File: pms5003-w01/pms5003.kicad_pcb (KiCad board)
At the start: 2 copper layers, 60 x 56 mm, 28 parts, among them J1 Battery, J2 DS3231, J3 PMS5003, J4 SHT10, J5 P2, J6 PROG, J7 USB_OTG, Q1 IRF540N, Q2 IRF7309IPBF, U1 U3V12F5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

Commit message: Next iteration of w01 pms5003
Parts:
- added C6: 22pF, Capacitors_SMD:C_0805, F.Cu at (166.0, 68.5)
- added C7: 1nF, Capacitors_SMD:C_0805, F.Cu at (139.1, 74.1)
- added R7: 10k, Resistors_SMD:R_1206, F.Cu at (139.0, 70.0)
- added SW1: SW_Push, Buttons_Switches_SMD:SW_SPST_B3S-1000, F.Cu at (167.0, 61.5)
- AE1: value Antenna -> Antenna_Shield; footprint various:Rainsun_AN9520 -> Connector_Coaxial:U.FL_Molex_MCRF_73412-0110_Vertical
- J2: footprint Socket_Strips:Socket_Strip_Straight_1x05_Pitch2.54mm -> various:DS3231
- J5: footprint Socket_Strips:Socket_Strip_Straight_1x02_Pitch2.54mm -> Pin_Headers:Pin_Header_Straight_1x02_Pitch2.54mm
- J7: footprint Connectors_USB:USB_Micro-B_Molex_47346-0001 -> various:USB_Micro-B_91-US01-517
- R2: value 100 -> 470
- moved J2 31.2 mm to (147.4, 40.8), turned to 90 degrees
- moved J4 14.4 mm to (143.4, 40.8), turned to 0 degrees
- moved AE1 4.03 mm to (168.0, 73.0), turned to 180 degrees
- moved J5 1.12 mm to (136.0, 75.5)
- moved C5 0.50 mm to (144.5, 54.5)
- moved R1 0.30 mm to (152.7, 55.0)
- moved J7 0.20 mm to (122.7, 52.5)
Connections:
- AE1 pad 2: (no net) -> -USB
- U11 pad 16: Net-(AE1-Pad1) -> Net-(C6-Pad1)
- U11 pad 2: (no net) -> RST
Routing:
- net RST: track 0.00 -> 43.0 mm
- net -USB: track 34.0 -> 51.0 mm
- net SHT10_SCK: track 7.25 -> 16.0 mm
- net SHT10_DATA: track 6.40 -> 13.1 mm
- net Net-(AE1-Pad1): track 9.66 -> 4.00 mm
- net RTC_SDA: track 21.5 -> 17.1 mm
- net Net-(J7-Pad6): track 10.8 -> 7.60 mm
- net Net-(C6-Pad1): track 0.00 -> 2.77 mm
- net 3V3: track 57.2 -> 59.8 mm, vias 0 -> 2
- net Net-(Q1-Pad1): track 28.6 -> 31.0 mm
- net +USB: track 47.0 -> 48.2 mm
- net P2: track 14.9 -> 16.0 mm
- net RTC_SCL: track 18.7 -> 17.7 mm
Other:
- board size 60 x 56 mm -> 53 x 54 mm
- net class USBCON added: clearance 0.2, trace_width 1, via_dia 0.4, via_drill 0.3
- board text added: "AIR QUALITY MONITOR V2.1"
- board text added: "Made in Poland"
- board text added: "©2018 www.kapusta.cc"

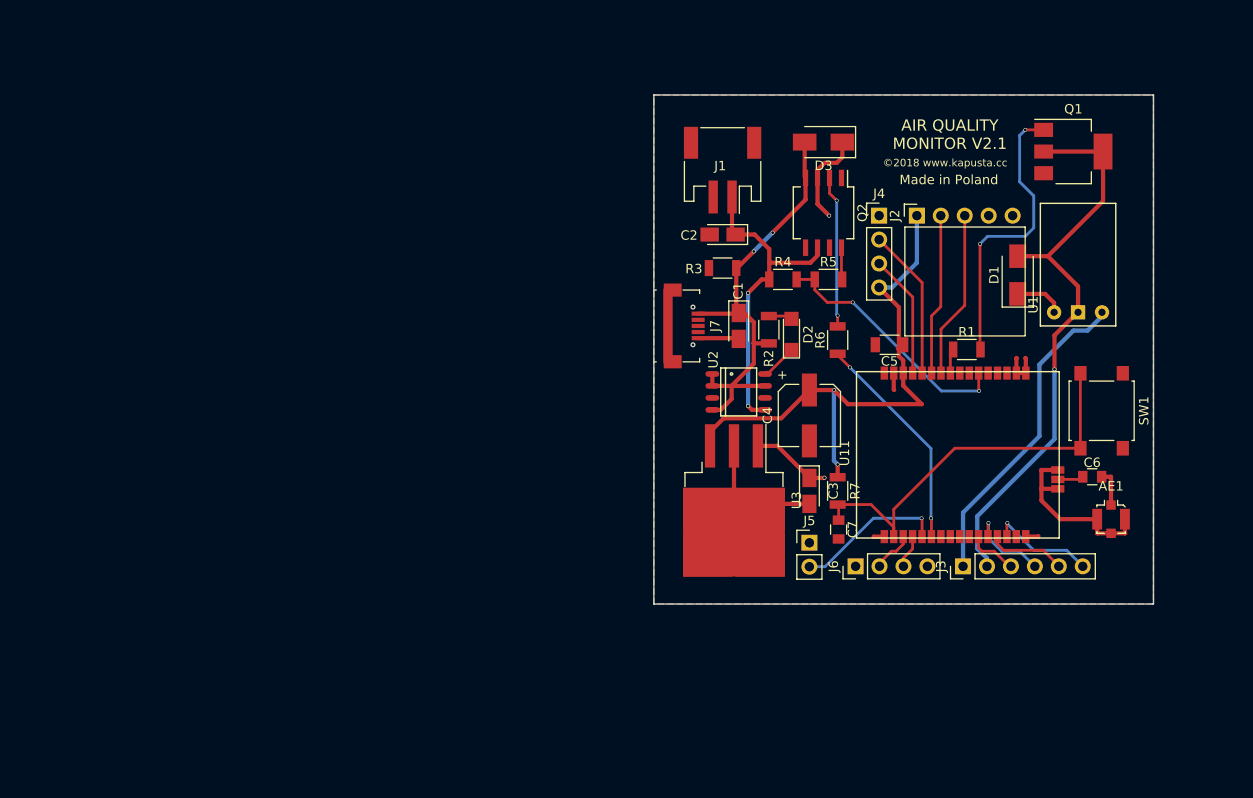
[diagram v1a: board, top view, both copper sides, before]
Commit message: W01 placement
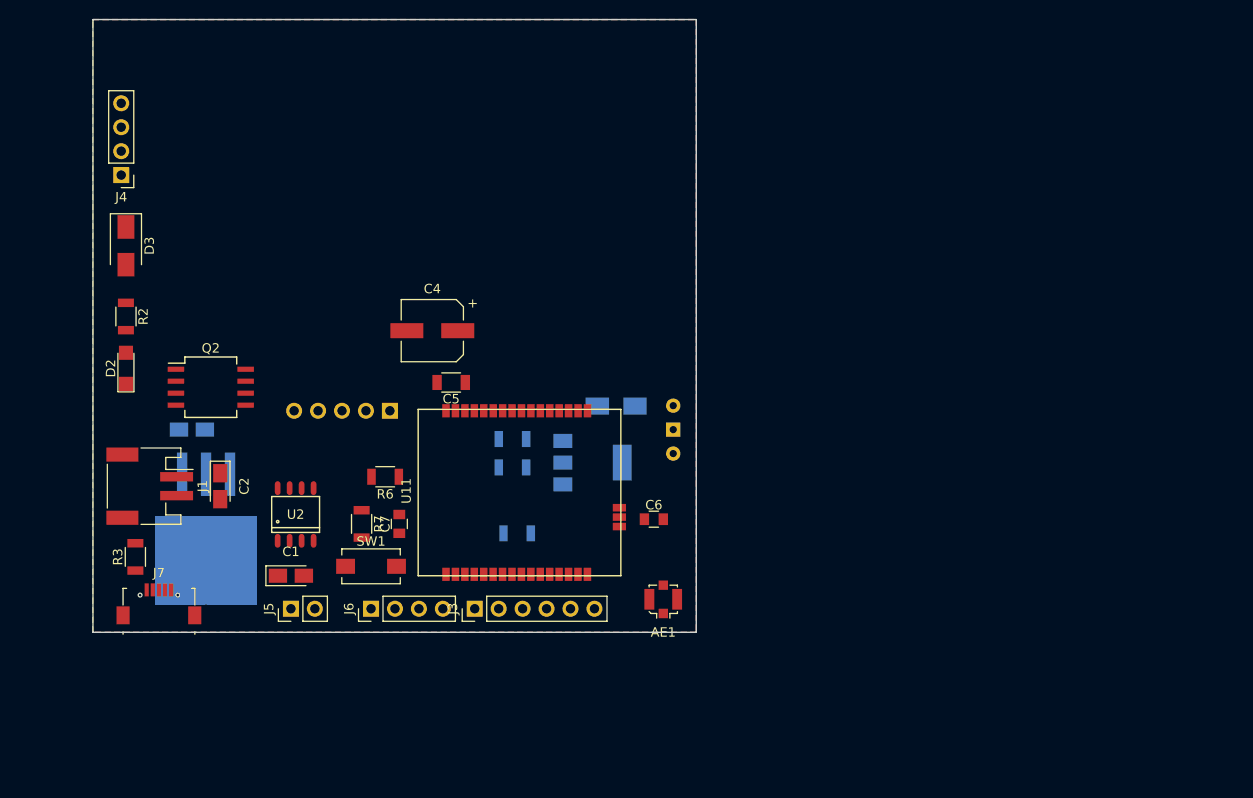
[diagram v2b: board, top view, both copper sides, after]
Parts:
- C3, D1, J2, Q1, R1, R4, R5, U1, U3: moved to B.Cu
- SW1: footprint Buttons_Switches_SMD:SW_SPST_B3S-1000 -> Buttons_Switches_SMD:SW_SPST_EVQPE1
- moved J4 80.5 mm to (63.0, 36.5), turned to 180 degrees
- moved SW1 79.2 mm to (89.5, 78.0), turned to 0 degrees
- moved D3 74.8 mm to (63.5, 44.0), turned to 270 degrees
- moved D2 70.7 mm to (63.5, 57.0)
- moved J1 69.4 mm to (66.0, 69.5), turned to 270 degrees
- moved R3 69.4 mm to (64.5, 77.0), turned to 90 degrees
- moved R2 68.2 mm to (63.5, 51.5), turned to 270 degrees
- moved Q2 67.6 mm to (72.5, 59.0), turned to 0 degrees
- moved C3 65.8 mm to (70.5, 63.5), turned to 0 degrees
- moved J7 63.0 mm to (67.0, 82.0), turned to 0 degrees
- moved Q1 60.7 mm to (113.0, 67.0)
- moved J2 59.6 mm to (91.5, 61.5)
- moved C2 59.6 mm to (73.5, 69.5), turned to 270 degrees
- moved U3 56.1 mm to (72.0, 74.0)
- moved J5 55.4 mm to (81.0, 82.5), turned to 90 degrees
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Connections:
- J2 pad 1: 3V3 -> SHT_RTC_VCC
- J4 pad 4: 3V3 -> SHT_RTC_VCC
- U11 pad 23: PMS_EN -> SHT_RTC_VCC
- U11 pad 7: (no net) -> PMS_EN
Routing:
- net 5V_GND: track 62.1 -> 0.00 mm, vias 1 -> 0
- net 3V3: track 59.8 -> 0.00 mm, vias 2 -> 0
- net -USB: track 51.0 -> 0.00 mm
- net +USB: track 48.2 -> 0.00 mm, vias 2 -> 0
- net RST: track 43.0 -> 0.00 mm
- net VBATT+: track 34.6 -> 0.00 mm, vias 2 -> 0
- net 5V: track 33.9 -> 0.00 mm
- net Net-(Q1-Pad1): track 31.0 -> 0.00 mm, vias 2 -> 0
- net ADC: track 26.8 -> 0.00 mm, vias 2 -> 0
- net VCC: track 23.9 -> 0.00 mm, vias 2 -> 0
- net ADC_EN: track 23.5 -> 0.00 mm, vias 2 -> 0
- net RTC_SCL: track 17.7 -> 0.00 mm
- net RTC_SDA: track 17.1 -> 0.00 mm
- net Net-(Q2-Pad2): track 16.1 -> 0.00 mm, vias 2 -> 0
- net SHT10_SCK: track 16.0 -> 0.00 mm
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- added copper zone on B.Cu, net 3V3
- removed copper zone on B.Cu, net VCC
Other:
- board size 53 x 54 mm -> 64 x 65 mm
- board text removed: "AIR QUALITY MONITOR V2.1"
- board text removed: "Made in Poland"
- board text removed: "©2018 www.kapusta.cc"

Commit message: Release PMS5003 in two versions
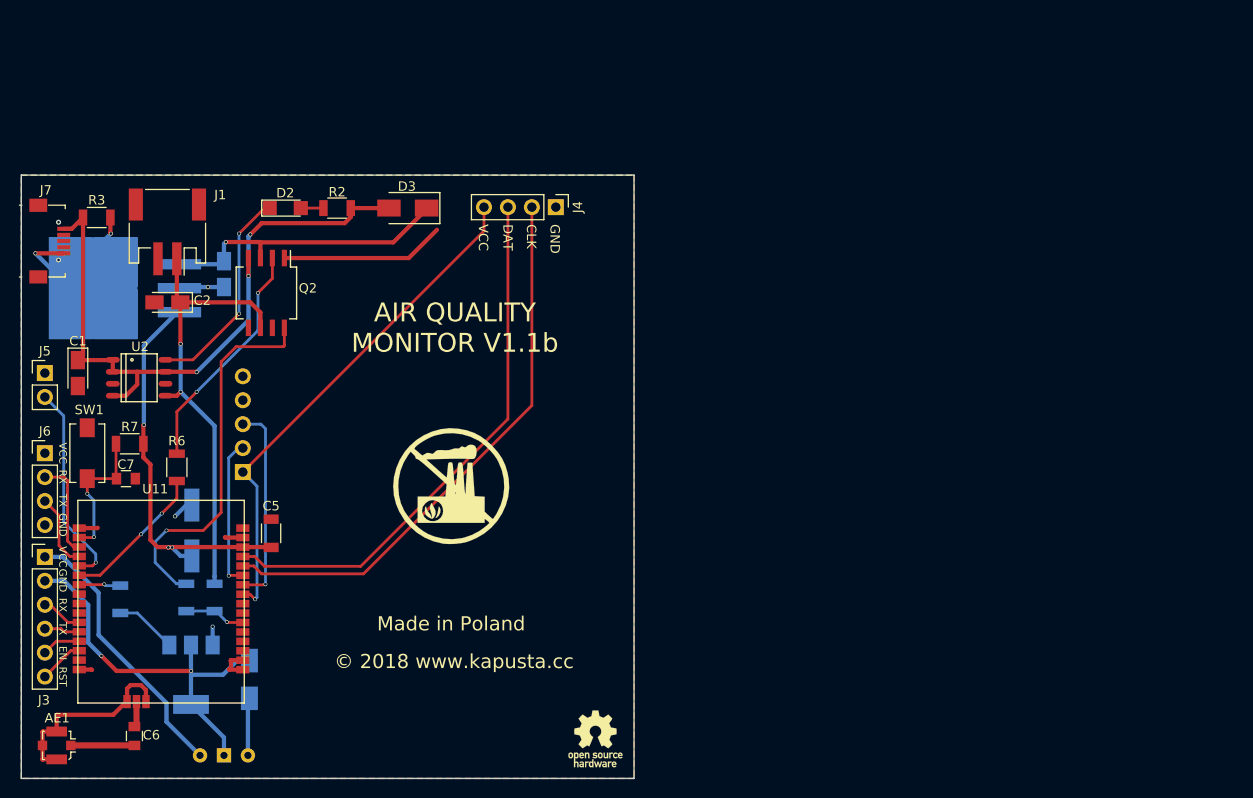
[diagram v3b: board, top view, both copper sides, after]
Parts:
- added G***: LOGO, various:pollution, F.Cu at (98.0, 69.5)
- added REF***: OSHW-Logo_5.7x6mm_SilkScreen, Symbols:OSHW-Logo_5.7x6mm_SilkScreen, F.Cu at (113.3, 96.3)
- C4: moved to B.Cu
- J4: footprint Pin_Headers:Pin_Header_Straight_1x04_Pitch2.54mm -> Socket_Strips:Socket_Strip_Straight_1x04_Pitch2.54mm
- J6: footprint Socket_Strips:Socket_Strip_Straight_1x04_Pitch2.54mm -> Pin_Headers:Pin_Header_Straight_1x04_Pitch2.54mm
- moved AE1 66.2 mm to (56.1, 97.0), turned to 90 degrees
- moved C6 59.7 mm to (64.4, 96.0), turned to 270 degrees
- moved D1 48.5 mm to (76.6, 90.0), turned to 90 degrees
- moved Q1 48.2 mm to (70.4, 89.5), turned to 270 degrees
- moved J4 46.2 mm to (109.1, 39.9), turned to 270 degrees
- moved J3 45.9 mm to (54.9, 77.0), turned to 0 degrees
- moved R1 42.7 mm to (62.9, 81.5), turned to 270 degrees
- moved U1 41.9 mm to (77.9, 86.5), turned to 270 degrees
- moved J7 40.2 mm to (55.4, 43.5), turned to 270 degrees
- moved J6 38.3 mm to (54.9, 66.0), turned to 0 degrees
- moved R5 37.3 mm to (69.9, 81.3), turned to 90 degrees
- moved U11 37.0 mm to (58.4, 71.0), turned to 0 degrees
- moved R3 36.2 mm to (60.4, 41.0), turned to 0 degrees
- moved J5 36.1 mm to (54.9, 57.5), turned to 0 degrees
- moved R4 35.8 mm to (72.9, 81.3), turned to 270 degrees
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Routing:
- net -USB: track 0.00 -> 76.6 mm, vias 0 -> 5
- net +USB: track 0.00 -> 71.5 mm, vias 0 -> 3
- net SHT10_SCK: track 0.00 -> 59.4 mm
- net SHT10_DATA: track 0.00 -> 57.5 mm
- net SHT_RTC_VCC: track 0.00 -> 54.4 mm, vias 0 -> 1
- net VBATT+: track 0.00 -> 48.5 mm, vias 0 -> 2
- net 3V3: track 0.00 -> 42.0 mm, vias 0 -> 3
- net 5V_GND: track 0.00 -> 41.8 mm, vias 0 -> 2
- net Net-(Q2-Pad8): track 0.00 -> 40.0 mm, vias 0 -> 1
- net VCC: track 0.00 -> 37.6 mm, vias 0 -> 1
- net 5V: track 0.00 -> 29.0 mm
- net Net-(Q2-Pad2): track 0.00 -> 24.9 mm, vias 0 -> 2
- net Net-(D2-Pad1): track 0.00 -> 22.7 mm, vias 0 -> 2
- net P2: track 0.00 -> 21.7 mm, vias 0 -> 1
- net RTC_SCL: track 0.00 -> 21.5 mm, vias 0 -> 1
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- added copper zone on B.Cu, net VCC
- removed copper zone on B.Cu, net 3V3
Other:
- board size 64 x 65 mm -> 65 x 64 mm
- net class Antenna added: clearance 0.2, trace_width 0.65, via_dia 0.4, via_drill 0.3
- board text added: "AIR QUALITY MONITOR V1.1b"
- board text added: "CLK"
- board text added: "DAT"
- board text added: "EN"
- board text added: "GND"
- board text added: "Made in Poland"
- board text added: "RST"
- board text added: "RX"
- board text added: "SCL"
- board text added: "SDA"
- board text added: "TX"
- board text added: "VCC"
- board text added: "VIN"
- board text added: "VOUT"
- board text added: "© 2018 www.kapusta.cc"
